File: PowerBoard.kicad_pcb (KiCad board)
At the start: 2 copper layers, 131 x 131 mm, 113 parts, among them J1 XT90, J10 DEAN_T, J11 DEAN_T, J12 DEAN_T, J13 DEAN_T, J14 DEAN_T, J15 DEAN_T, J16 XT60, J17 XT60, J18 XT60, J19 XT60, J2 DEAN_T, J20 XT60, J21 XT60, J22 XT30, J23 XT30, J24 XT30, J25 XT30, J26 XT30, J27 XT30, J28 XT90, J29 XT30, J3 XT60, J30 XT30, J31 XT30, J32 Conn_01x02, J4 XT30, J5 XT90, J6 XT90, J7 XT90, J8 XT90, J9 XT90, Q1 IRF9540N, Q2 IRF9540N, Q3 BC817, Q4 BC817, Q5 IRF9540N, Q6 BC817, Q7 IRF9540N, Q8 BC817, U1 Pico, U2 LM317_TO-220

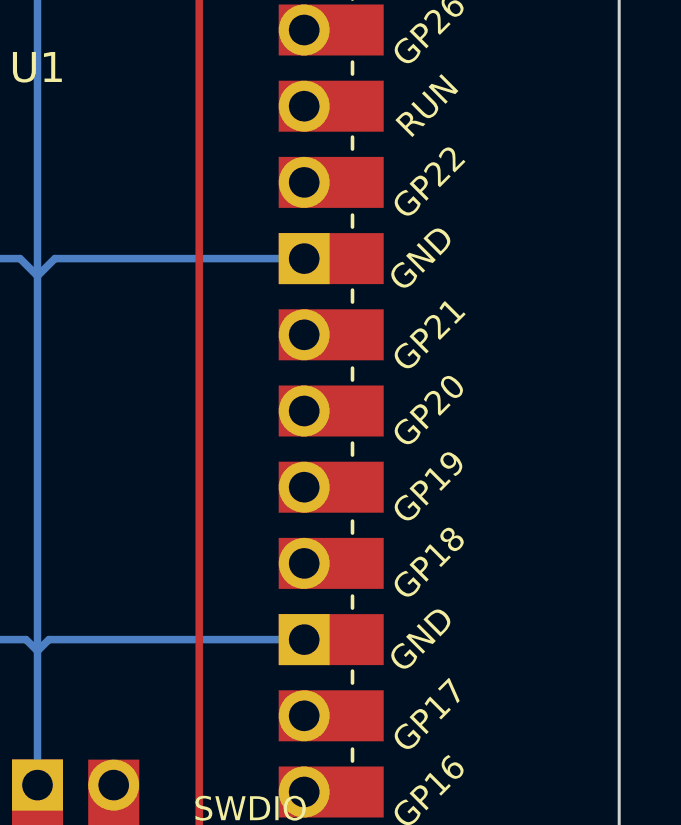
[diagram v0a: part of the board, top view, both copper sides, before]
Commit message: added status leds
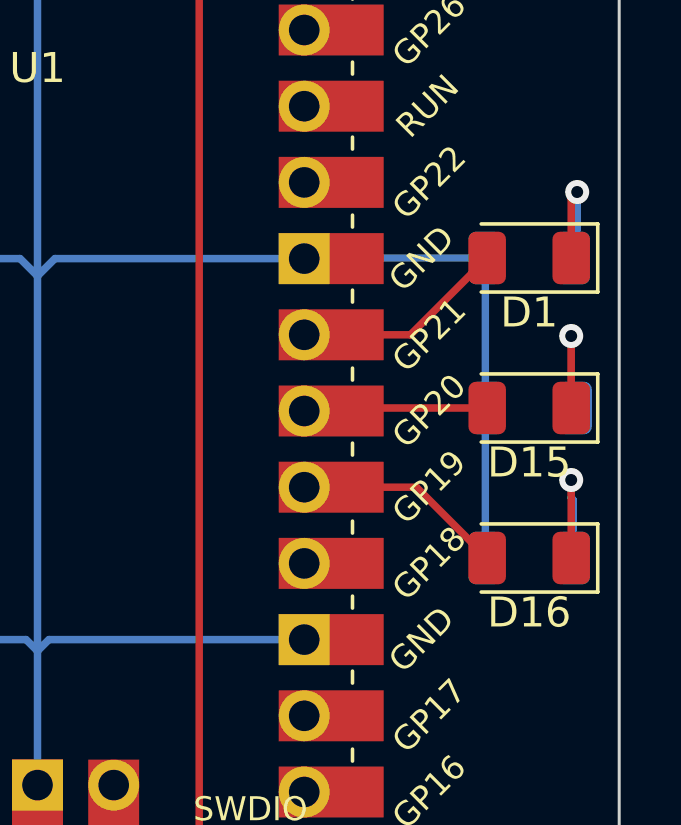
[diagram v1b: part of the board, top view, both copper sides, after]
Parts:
- added D1: LED, Diode_SMD:D_1206_3216Metric, F.Cu at (208.0, 94.4)
- added D15: LED, Diode_SMD:D_1206_3216Metric, F.Cu at (208.0, 99.4)
- added D16: LED, Diode_SMD:D_1206_3216Metric, F.Cu at (208.0, 104.4)
- added R33: 10k, Resistor_SMD:R_1206_3216Metric, B.Cu at (208.0, 94.4)
- added R39: 10k, Resistor_SMD:R_1206_3216Metric, B.Cu at (208.1, 99.4)
- added R40: 10k, Resistor_SMD:R_1206_3216Metric, B.Cu at (208.0, 104.4)
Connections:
- U1 pad 25: unconnected-(U1-GPIO19-Pad25)_1 -> Net-(D16-A)
- U1 pad 26: unconnected-(U1-GPIO20-Pad26) -> Net-(D15-A)
- U1 pad 27: unconnected-(U1-GPIO21-Pad27)_1 -> Net-(D1-A)
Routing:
- net GND: track 1017.5 -> 1033.5 mm
- net Net-(D1-A): track 0.00 -> 7.16 mm
- net Net-(D16-A): track 0.00 -> 7.08 mm
- net Net-(D15-A): track 0.00 -> 6.14 mm
- net Net-(D16-K): track 0.00 -> 5.23 mm, vias 0 -> 1
- net Net-(D15-K): track 0.00 -> 4.85 mm, vias 0 -> 1
- net Net-(D1-K): track 0.00 -> 4.54 mm, vias 0 -> 1

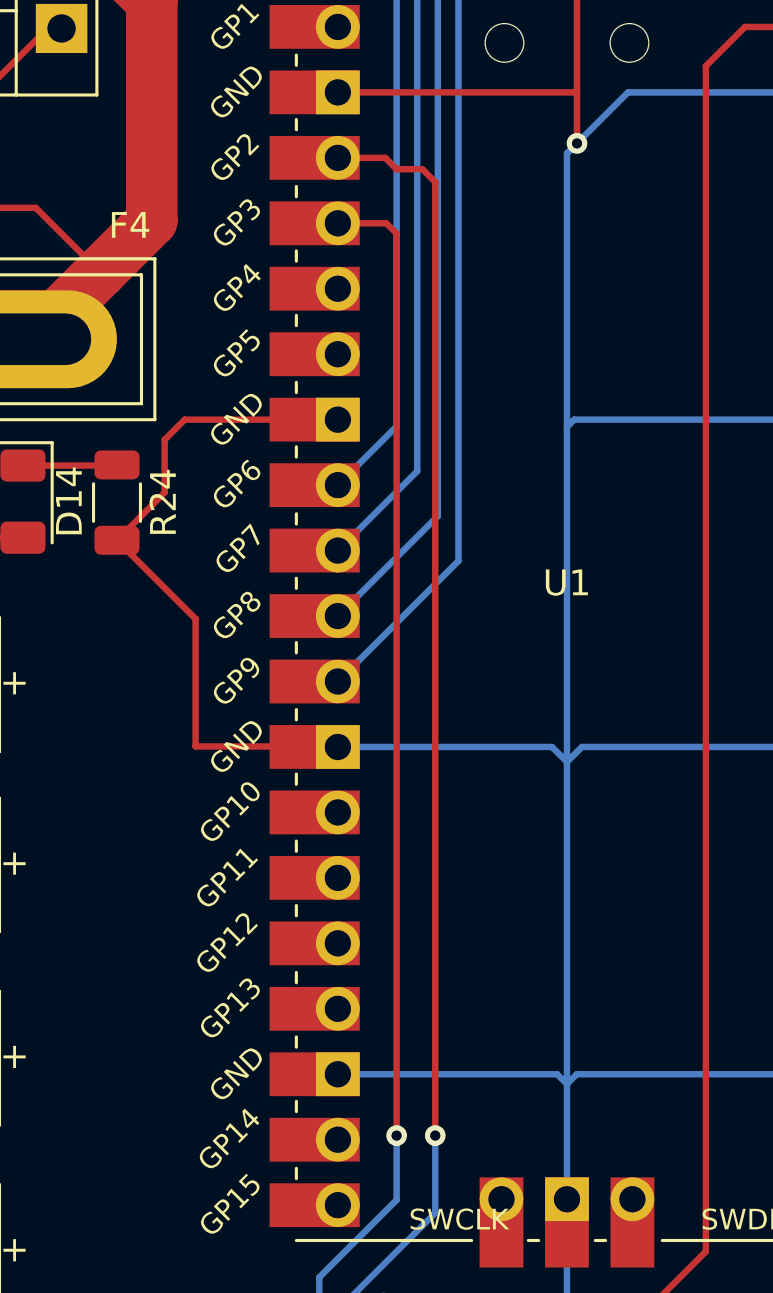
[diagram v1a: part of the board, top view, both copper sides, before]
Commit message: changed i2c connection
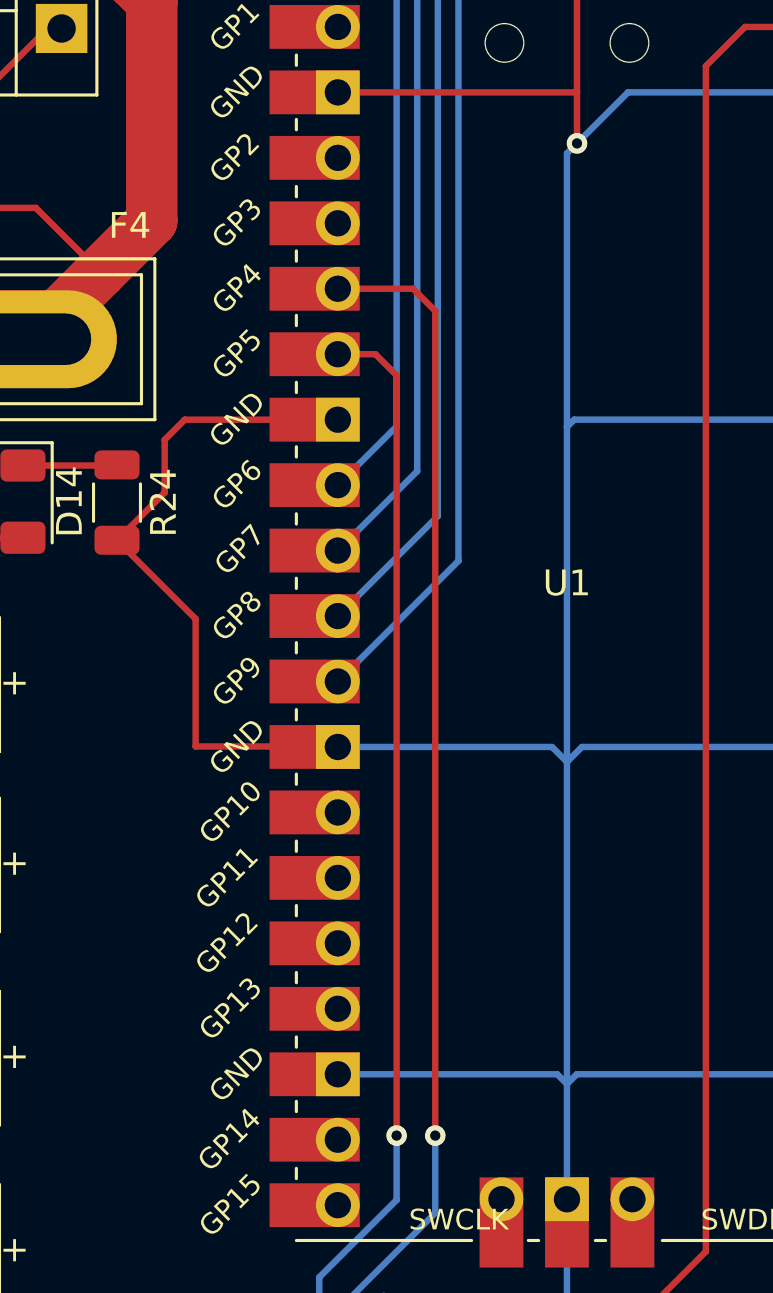
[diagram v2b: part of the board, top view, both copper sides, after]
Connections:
- U1 pad 4: SDA -> unconnected-(U1-GPIO2-Pad4)
- U1 pad 5: SCL -> unconnected-(U1-GPIO3-Pad5)
- U1 pad 6: unconnected-(U1-GPIO4-Pad6)_1 -> SDA
- U1 pad 7: unconnected-(U1-GPIO5-Pad7)_1 -> SCL
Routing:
- net SCL: track 75.4 -> 70.1 mm
- net SDA: track 82.3 -> 77.2 mm

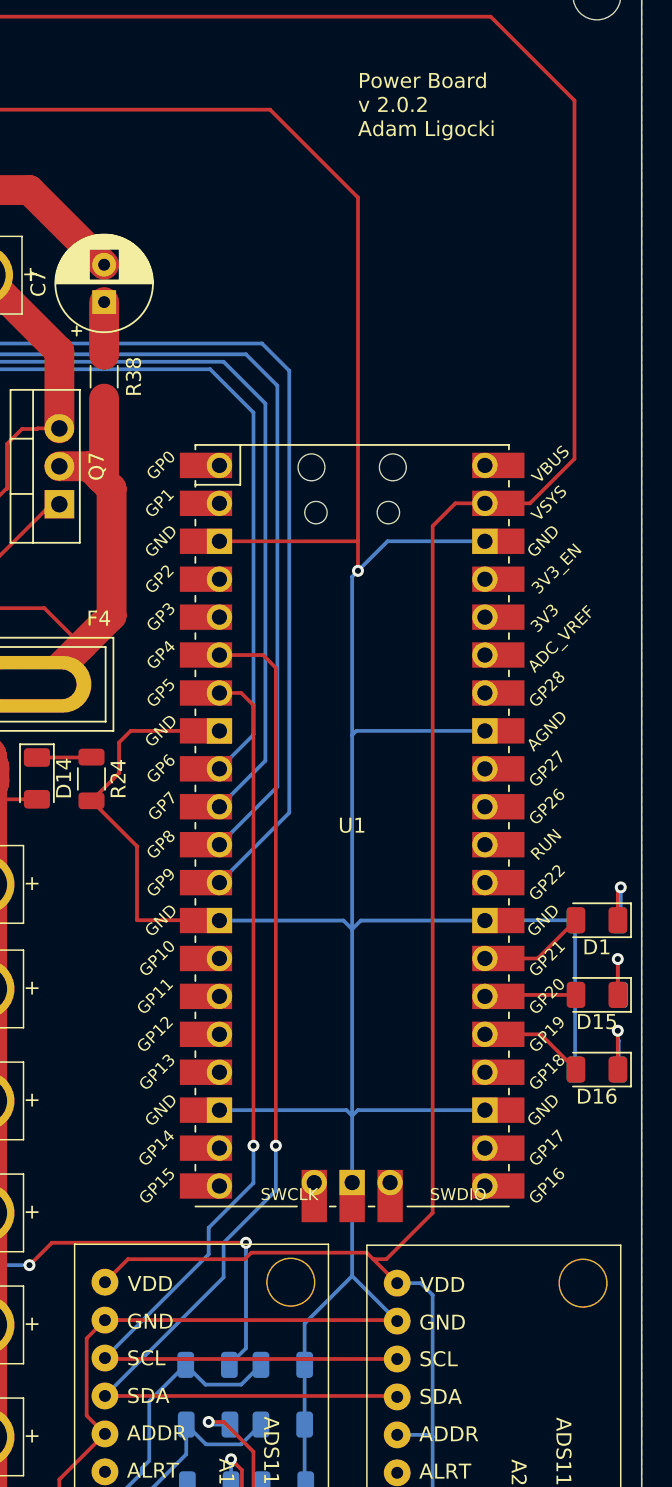
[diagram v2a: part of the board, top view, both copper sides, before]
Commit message: added spi and i2c terminals
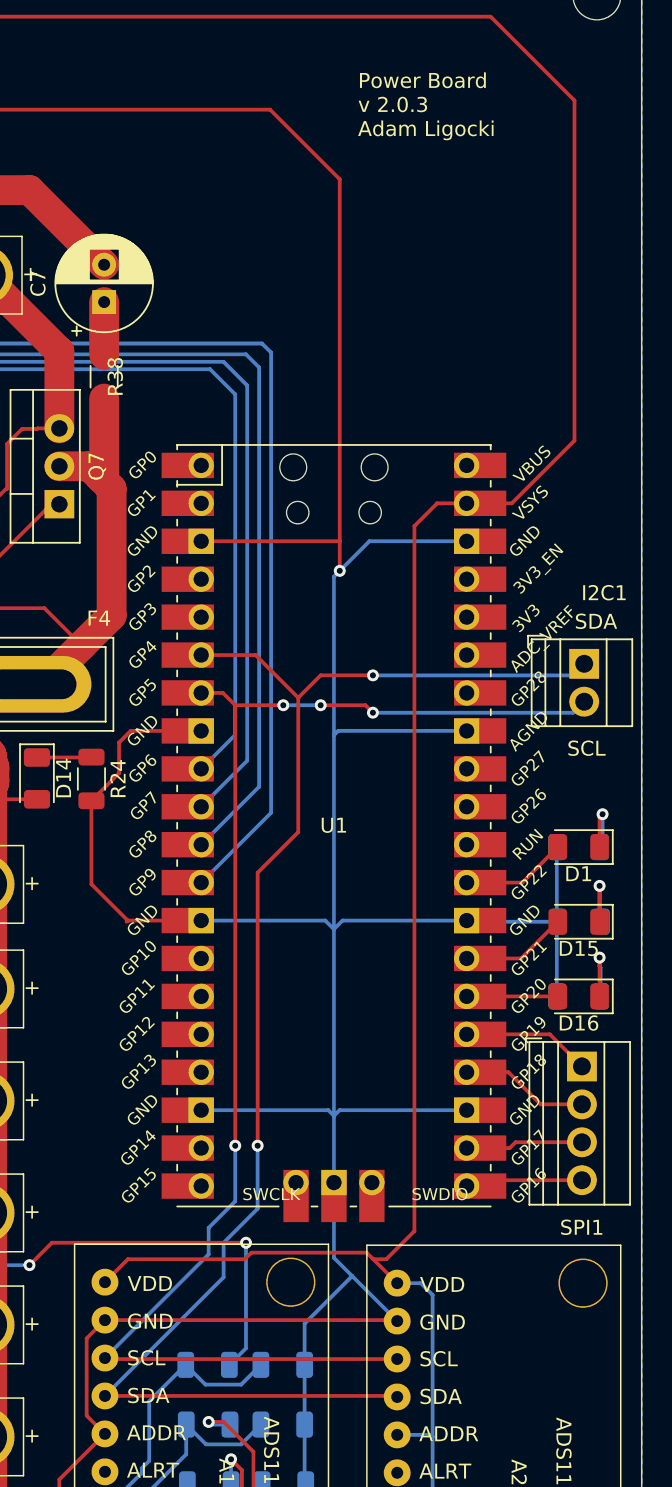
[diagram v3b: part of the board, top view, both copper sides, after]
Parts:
- added I2C1: Screw_Terminal_01x02, TerminalBlock:TerminalBlock_Xinya_XY308-2.54-2P_1x02_P2.54mm_Horizontal, F.Cu at (207.2, 77.2)
- added SPI1: Screw_Terminal_01x04, TerminalBlock:TerminalBlock_Xinya_XY308-2.54-4P_1x04_P2.54mm_Horizontal, F.Cu at (207.0, 104.2)
- moved D1 5.05 mm to (206.8, 89.5)
- moved D15 5.05 mm to (206.8, 94.5)
- moved D16 5.05 mm to (206.8, 99.5)
- moved R33 5.05 mm to (206.8, 89.5)
- moved R39 5.05 mm to (206.8, 94.5)
- moved R40 5.05 mm to (206.8, 99.5)
- moved U1 1.22 mm to (190.4, 88.1)
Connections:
- U1 pad 21: unconnected-(U1-GPIO16-Pad21) -> Net-(SPI1-Pin_4)
- U1 pad 22: unconnected-(U1-GPIO17-Pad22) -> Net-(SPI1-Pin_3)
- U1 pad 24: unconnected-(U1-GPIO18-Pad24) -> Net-(SPI1-Pin_2)
- U1 pad 25: Net-(D16-A) -> Net-(SPI1-Pin_1)
- U1 pad 26: Net-(D15-A) -> Net-(D16-A)
- U1 pad 27: Net-(D1-A) -> Net-(D15-A)
- U1 pad 29: unconnected-(U1-GPIO22-Pad29) -> Net-(D1-A)
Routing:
- net SCL: track 70.1 -> 93.4 mm, vias 1 -> 4
- net SDA: track 77.2 -> 99.5 mm, vias 1 -> 2
- net Net-(SPI1-Pin_2): track 0.00 -> 8.61 mm
- net Net-(SPI1-Pin_1): track 0.00 -> 8.61 mm
- net Net-(SPI1-Pin_4): track 0.00 -> 7.88 mm
- net Net-(SPI1-Pin_3): track 0.00 -> 7.88 mm
- net Net-(D15-A): track 6.14 -> 7.12 mm
- net Net-(D16-A): track 7.08 -> 6.24 mm
- net EN_12V: track 91.8 -> 91.3 mm
- net EN_5V: track 73.6 -> 73.1 mm
- net EN_48V: track 129.0 -> 128.5 mm
- net EN_24V: track 106.3 -> 105.8 mm
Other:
- board text added: "Power Board v 2.0.3 Adam Ligocki"
- board text added: "SCL"
- board text added: "SDA"
- board text removed: "Power Board v 2.0.2 Adam Ligocki"

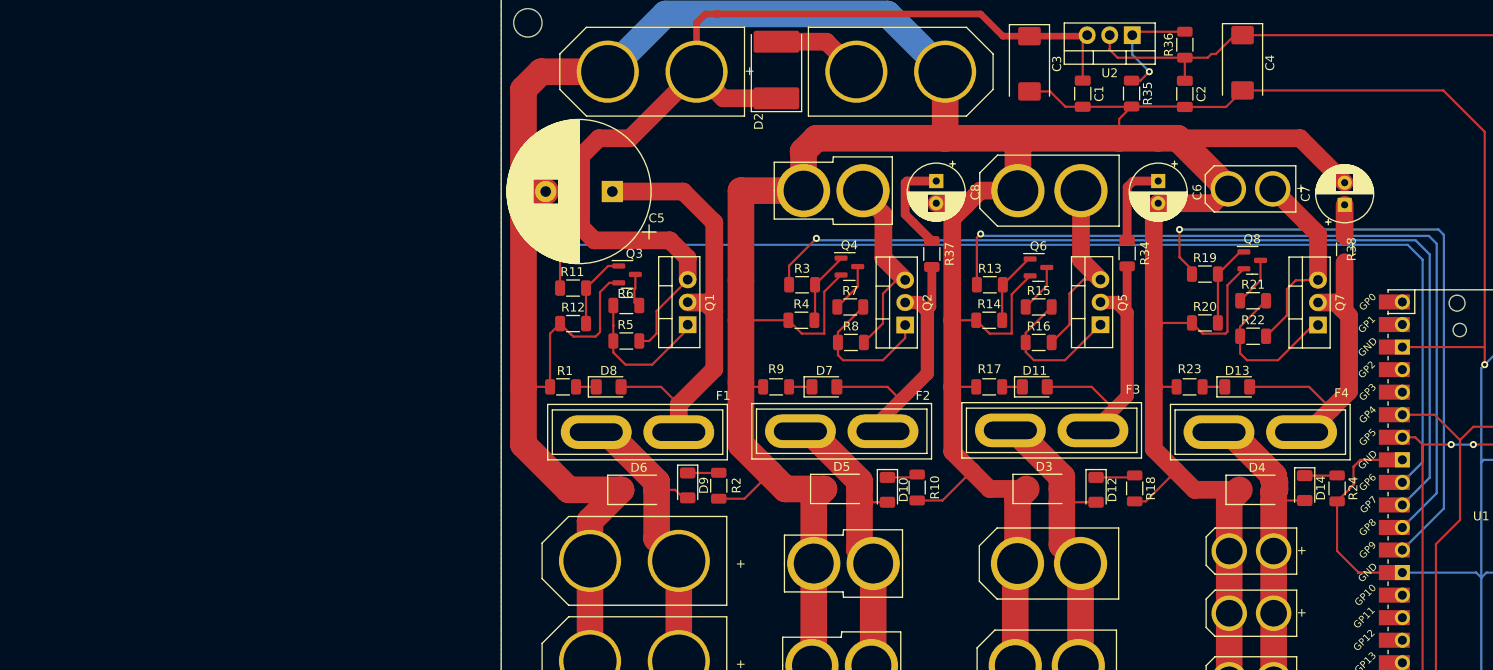
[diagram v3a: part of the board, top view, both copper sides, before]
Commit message: Add LTC7004 driver
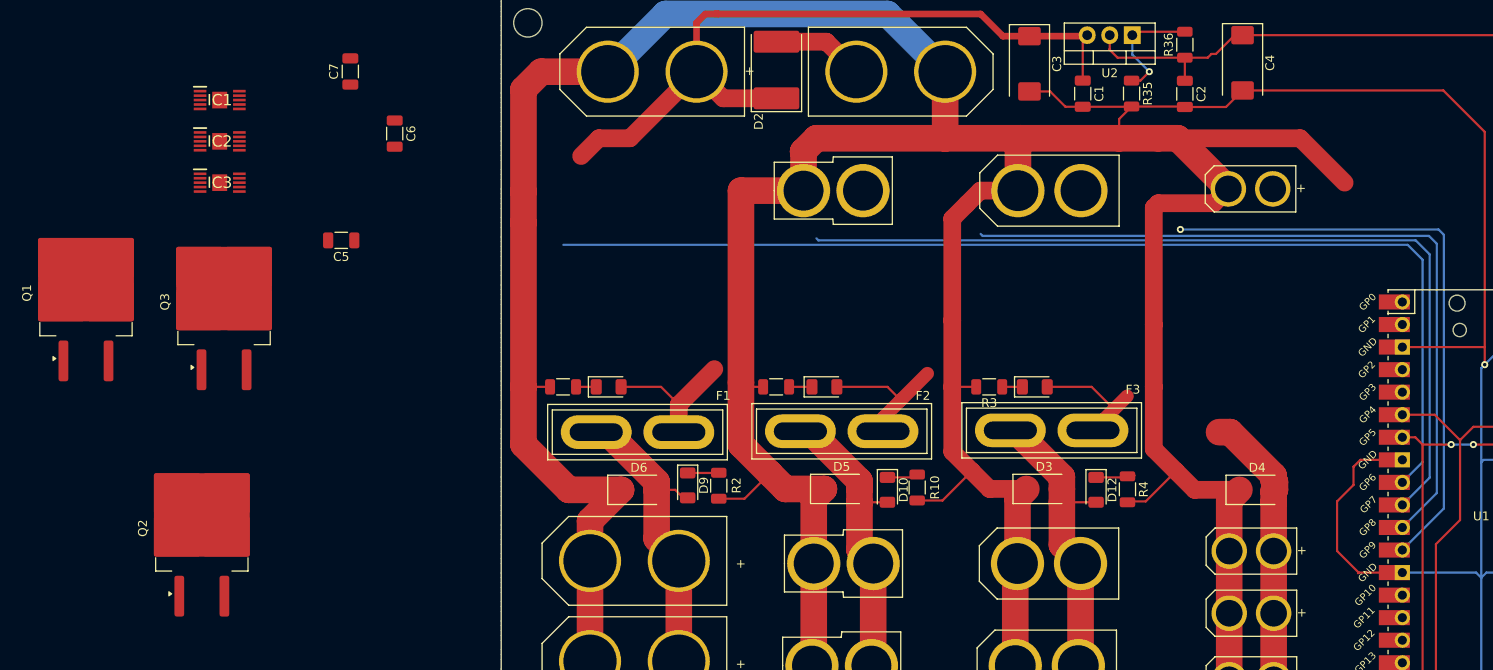
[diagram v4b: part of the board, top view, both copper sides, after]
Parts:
- removed C8: 47u, Capacitor_THT:CP_Radial_D6.3mm_P2.50mm
- removed D13, D14: LED, Diode_SMD:D_1206_3216Metric
- removed F4: Fuse, Fuse:Fuse_Blade_ATO_directSolder
- removed Q4, Q6, Q8: BC817, Package_TO_SOT_SMD:SOT-23
- removed Q5, Q7: IRF9540N, Package_TO_SOT_THT:TO-220-3_Vertical
- removed R11, R13, R16, R19, R22, R5, R8: 10k, Resistor_SMD:R_1206_3216Metric
- removed R12, R14, R20: 100k, Resistor_SMD:R_1206_3216Metric
- removed R15, R21, R6, R7: 22R, Resistor_SMD:R_1206_3216Metric
- removed R17, R18: 3k3, Resistor_SMD:R_1206_3216Metric
- removed R23, R24, R34, R37, R38: 1k, Resistor_SMD:R_1206_3216Metric
- added IC1: LTC7004HMSE#PBF, SamacSys_Parts:SOP50P490X110-11N, F.Cu at (48.3, 41.2)
- added IC2: LTC7004HMSE#PBF, SamacSys_Parts:SOP50P490X110-11N, F.Cu at (48.3, 45.8)
- added IC3: LTC7004HMSE#PBF, SamacSys_Parts:SOP50P490X110-11N, F.Cu at (48.3, 50.5)
- C5: value 1m -> 0.1u; footprint Capacitor_THT:CP_Radial_D16.0mm_P7.50mm -> Capacitor_SMD:C_1206_3216Metric
- C6, C7: value 47u -> 0.1u; footprint Capacitor_THT:CP_Radial_D6.3mm_P2.50mm -> Capacitor_SMD:C_1206_3216Metric
- Q1, Q2: value IRF9540N -> IRFS7437TRLPBF; footprint Package_TO_SOT_THT:TO-220-3_Vertical -> Package_TO_SOT_SMD:TO-263-2
- Q3: value BC817 -> IRFS7437TRLPBF; footprint Package_TO_SOT_SMD:SOT-23 -> Package_TO_SOT_SMD:TO-263-2
- R1, R2: value 15k -> 6k8
- R3: value 10k -> 6k8
- R4: value 100k -> 6k8
- moved C7 113.0 mm to (63.0, 38.0)
- moved C6 86.2 mm to (68.0, 45.0)
- moved Q2 82.5 mm to (46.3, 89.4)
- moved Q1 67.9 mm to (33.2, 62.9)
- moved Q3 45.5 mm to (48.8, 63.9), turned to 90 degrees
- moved R4 41.4 mm to (150.5, 85.0), turned to -90 degrees
- moved C5 31.0 mm to (62.0, 57.0)
- moved R3 24.0 mm to (135.0, 73.5), turned to 180 degrees
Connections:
- C1 pad 1: +48V -> +42V
- C3 pad 1: +48V -> +42V
- C5 pad 1: Net-(D8-A) -> Net-(IC1-BST)
- C5 pad 2: GND -> Net-(IC1-TS)
- C6 pad 2: GND -> Net-(IC2-TS)
- C7 pad 2: GND -> Net-(IC3-TS)
- D2 pad 1: +48V -> +42V
- D6 pad 2: 48V_2 -> 42V_2
- D9 pad 2: 48V_2 -> 5V_2
- F1 pad 2: 48V_2 -> 5V_2
- J1 pad 1: +48V -> +42V
- J28 pad 1: 48V_2 -> 42V_2
- J5 pad 1: 48V_2 -> 42V_2
- J6 pad 1: 48V_2 -> 42V_2
- J7 pad 1: 48V_2 -> 42V_2
- J8 pad 1: 48V_2 -> 42V_2
- J9 pad 1: 48V_2 -> 42V_2
- Q1 pad 2: Net-(D8-A) -> Net-(D7-A)
- Q1 pad 3: +48V -> +24V
- Q2 pad 2: Net-(D7-A) -> Net-(D8-A)
- Q2 pad 3: +24V -> +5V
- Q3 pad 2: GND -> Net-(D11-A)
- Q3 pad 3: Net-(Q3-C) -> +12V
- R25 pad 1: 48V_2 -> 42V_2
- R3 pad 1: EN_24V -> Net-(D11-K)
- R3 pad 2: Net-(Q4-B) -> GND
- R4 pad 1: GND -> Net-(D12-K)
- R4 pad 2: Net-(Q4-B) -> GND
- U2 pad 3: +48V -> +42V
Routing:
- net 48V_2: track 177.6 -> 0.00 mm, vias 2 -> 0
- net 5V_2: track 104.7 -> 279.0 mm, vias 2 -> 4
- net +48V: track 117.6 -> 0.00 mm
- net +42V: track 0.00 -> 84.0 mm
- net GND: track 1033.8 -> 954.6 mm
- net Net-(D13-A): track 36.9 -> 0.00 mm
- net Net-(D8-A): track 48.9 -> 16.1 mm
- net +5V: track 22.6 -> 0.00 mm
- net +12V: track 21.4 -> 0.00 mm
- net +24V: track 21.6 -> 0.35 mm
- net Net-(D11-A): track 32.1 -> 14.0 mm
- net Net-(Q7-G): track 17.9 -> 0.00 mm
- net Net-(IC2-TGDN): track 16.9 -> 0.00 mm
- net Net-(Q5-G): track 16.8 -> 0.00 mm
- net Net-(IC1-TGDN): track 16.4 -> 0.00 mm
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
